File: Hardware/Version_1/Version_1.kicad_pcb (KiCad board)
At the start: 6 copper layers, 65 x 30 mm, 98 parts, among them IC1 LIFCL-40-7BG256C, IC2 W25R256JVEIQ, IC3 IS46TR16128D-125KBLA2, IC4 TPS62A01DRLR, IC5 TPS62A01DRLR, IC6 TPS62A01DRLR, J1 GPIO, J2 Conn_01x05_Pin, J3 52435-2271, J4 52435-2271, U1 CAT24C256, Y1 AK3ADDF1-156.2500T3

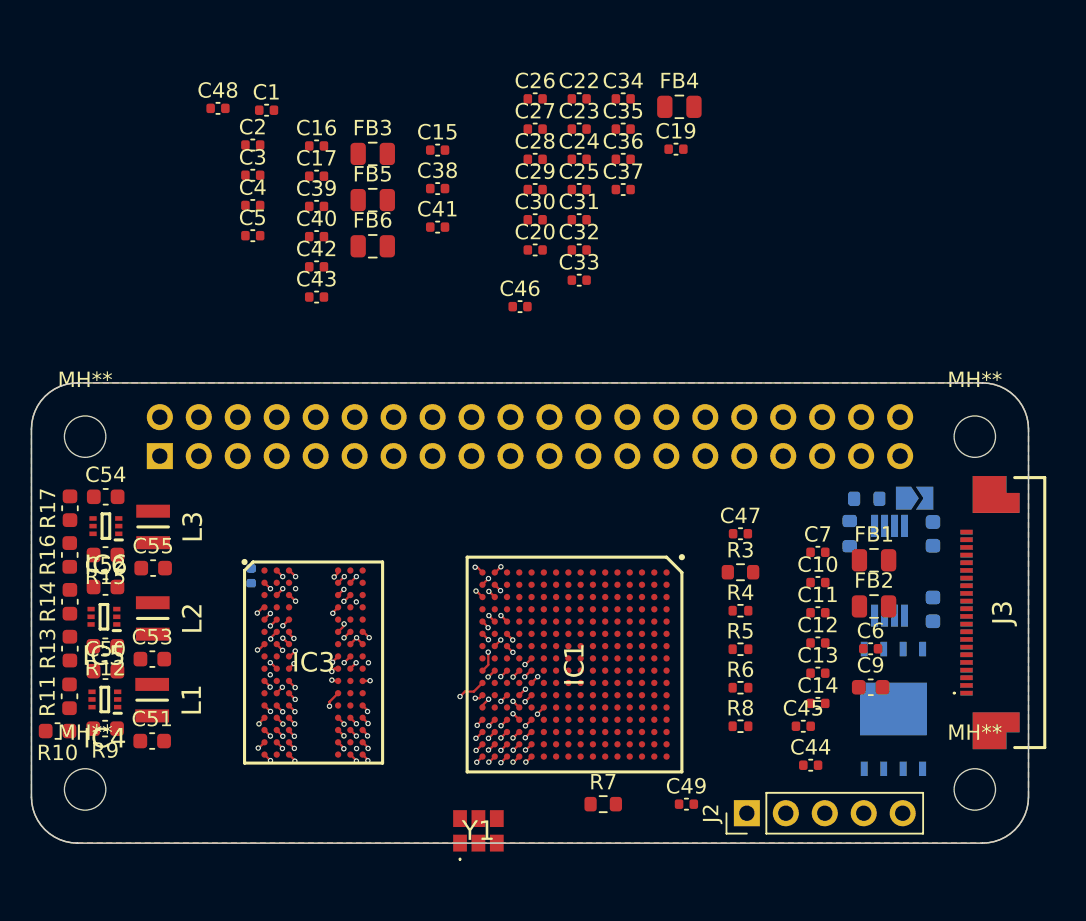
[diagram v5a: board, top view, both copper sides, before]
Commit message: mipi routing
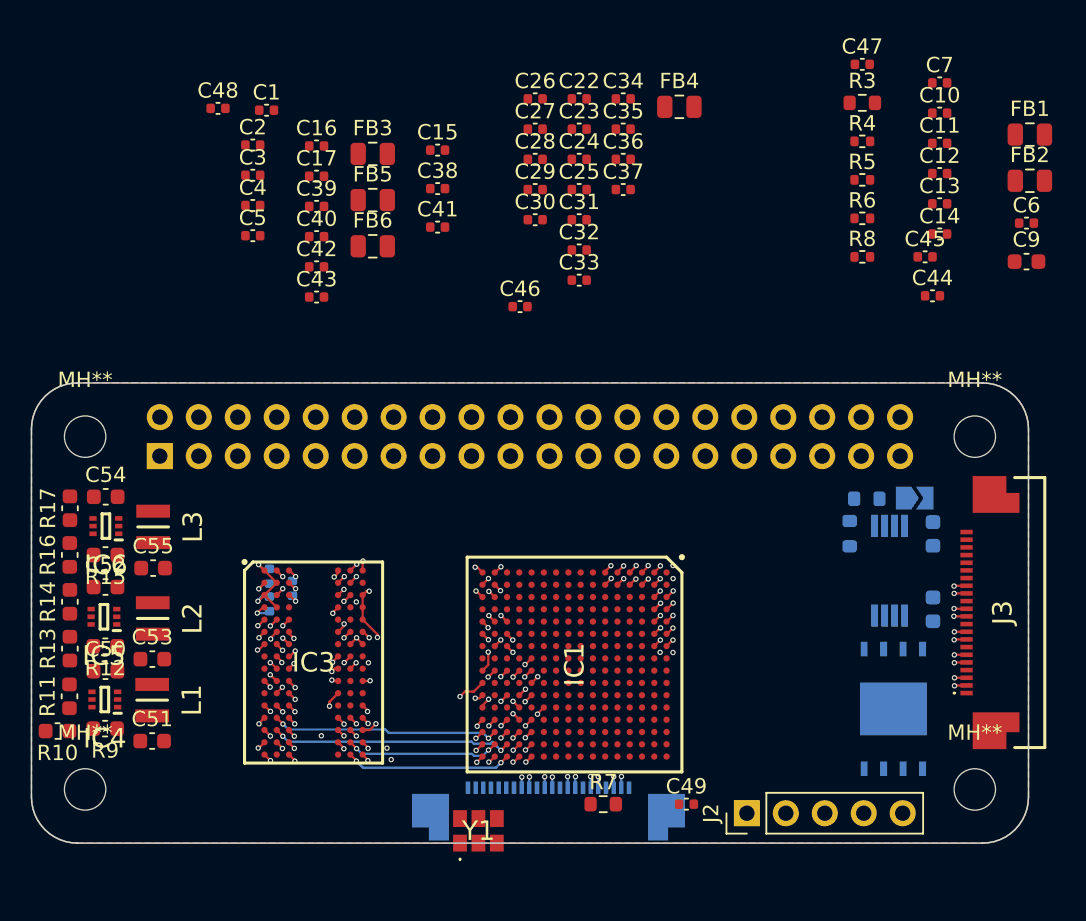
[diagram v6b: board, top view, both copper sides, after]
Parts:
- C19, C20: moved to B.Cu
- moved C19 39.8 mm to (115.5, 84.4), turned to -90 degrees
- moved J4 32.9 mm to (133.7, 98.9), turned to 180 degrees
- moved C10 31.6 mm to (159.2, 52.4)
- moved C44 31.6 mm to (158.7, 64.3)
- moved C7 31.6 mm to (159.2, 50.4)
- moved C11 31.6 mm to (159.2, 54.4)
- moved C12 31.6 mm to (159.2, 56.4)
- moved C13 31.6 mm to (159.2, 58.3)
- moved C14 31.6 mm to (159.2, 60.3)
- moved C47 31.6 mm to (154.2, 49.2)
- moved R3 31.6 mm to (154.2, 51.7)
- moved R5 31.6 mm to (154.2, 56.8)
- moved R6 31.6 mm to (154.2, 59.3)
- moved C45 31.6 mm to (158.3, 61.8)
- moved R4 31.6 mm to (154.2, 54.2)
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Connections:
- IC1 pad E1: /CSI2_D3_P -> /CSI1_D0_P
- IC1 pad E2: /CSI2_D3_P -> /CSI1_D0_N
- J3 pad 11: /CSI1_D2_N -> /CSI2_D0_N
- J3 pad 12: /CSI1_D2_P -> /CSI2_D0_P
- J3 pad 14: /CSI1_D3_N -> /CSI2_D2_N
- J3 pad 15: /CSI1_D3_P -> /CSI2_D2_P
- J3 pad 2: /CSI1_D0_N -> /CSI2_D3_N
- J3 pad 20: /CSI1_SCL -> /CSI2_SCL
- J3 pad 21: /CSI1_SDA -> /CSI2_SDA
- J3 pad 3: /CSI1_D0_P -> /CSI2_D3_P
- J3 pad 5: /CSI1_D1_N -> /CSI2_D1_N
- J3 pad 6: /CSI1_D1_P -> /CSI2_D1_P
- J3 pad 8: /CSI1_CK_N -> /CSI2_CK_N
- J3 pad 9: /CSI1_CK_P -> /CSI2_CK_P
- J4 pad 11: /CSI2_D2_N -> /CSI1_D0_N
- J4 pad 12: /CSI2_D2_P -> /CSI1_D0_P
- J4 pad 14: /CSI2_D3_N -> /CSI1_D2_N
- J4 pad 15: /CSI2_D3_P -> /CSI1_D2_P
- J4 pad 2: /CSI2_D0_N -> /CSI1_D3_N
- J4 pad 20: /CSI2_SCL -> /CSI1_SCL
- J4 pad 21: /CSI2_SDA -> /CSI1_SDA
- J4 pad 3: /CSI2_D0_P -> /CSI1_D3_P
- J4 pad 5: /CSI2_D1_N -> /CSI1_D1_N
- J4 pad 6: /CSI2_D1_P -> /CSI1_D1_P
- J4 pad 8: /CSI2_CK_N -> /CSI1_CK_N
- J4 pad 9: /CSI2_CK_P -> /CSI1_CK_P
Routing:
- net /CSI2_D3_N: track 0.00 -> 21.8 mm, vias 0 -> 2
- net /CSI2_D1_N: track 0.00 -> 21.5 mm, vias 0 -> 2
- net /CSI2_CK_N: track 0.00 -> 21.3 mm, vias 0 -> 2
- net /CSI2_D0_N: track 0.00 -> 21.0 mm, vias 0 -> 2
- net /CSI2_D2_N: track 0.00 -> 20.7 mm, vias 0 -> 2
- net /CSI2_D3_P: track 0.00 -> 20.7 mm, vias 0 -> 2
- net /CSI2_D1_P: track 0.00 -> 20.5 mm, vias 0 -> 2
- net /CSI2_CK_P: track 0.00 -> 20.2 mm, vias 0 -> 2
- net /CSI2_D0_P: track 0.00 -> 19.9 mm, vias 0 -> 2
- net /CSI2_D2_P: track 0.00 -> 19.9 mm, vias 0 -> 2
- net /CSI1_D2_P: track 0.00 -> 17.6 mm, vias 0 -> 2
- net /CSI1_D0_P: track 0.00 -> 17.3 mm, vias 0 -> 2
- net /CSI1_CK_P: track 0.00 -> 17.0 mm, vias 0 -> 2
- net /CSI1_D1_P: track 0.00 -> 16.7 mm, vias 0 -> 2
- net /CSI1_D2_N: track 0.00 -> 16.5 mm, vias 0 -> 2
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- added copper zone on In3.Cu, net /VCCDRAM

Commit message: Added i2c and flash chip
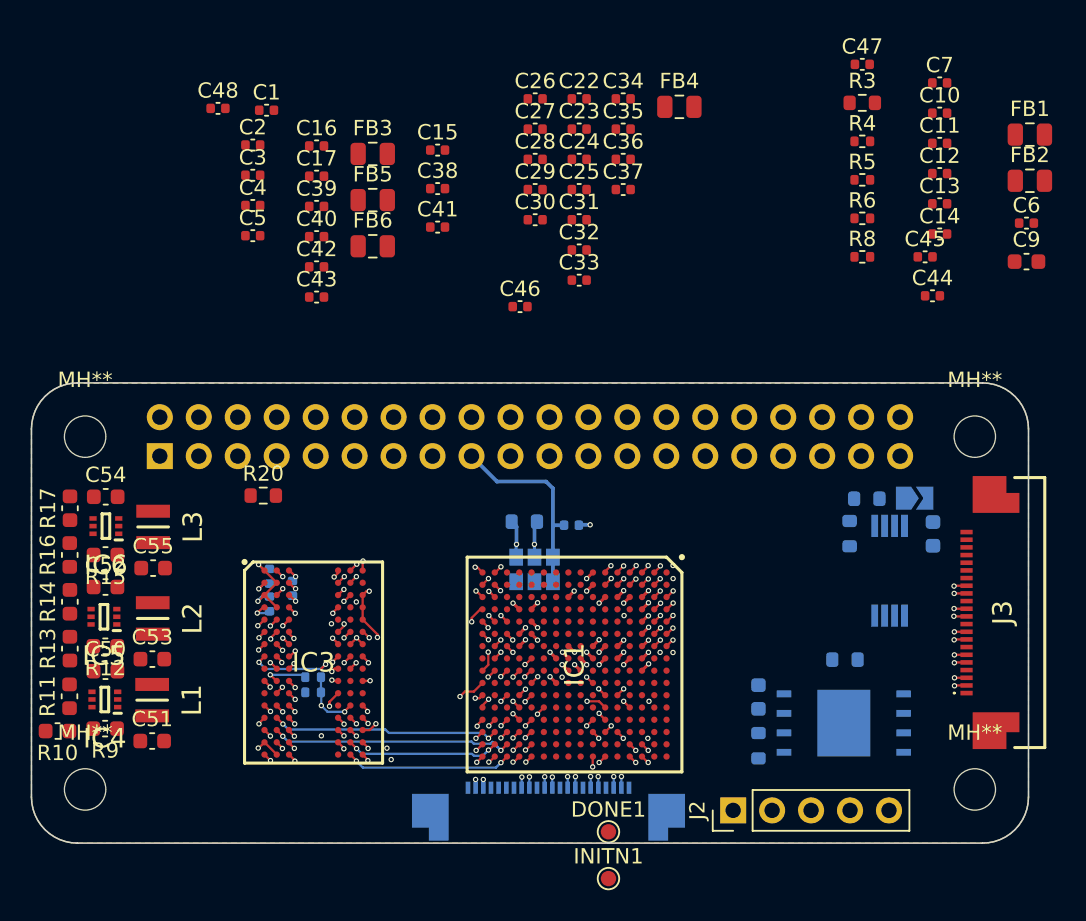
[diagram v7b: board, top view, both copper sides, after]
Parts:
- removed J1: GPIO, Connector_PinSocket_2.54mm:PinSocket_2x20_P2.54mm_Vertical
- added DONE1: TestPoint, TestPoint:TestPoint_Pad_D1.0mm, F.Cu at (137.6, 99.3)
- added INITN1: TestPoint, TestPoint:TestPoint_Pad_D1.0mm, F.Cu at (137.6, 102.3)
- added J6: GPIO, Connector_PinSocket_2.54mm:PinSocket_2x20_P2.54mm_Vertical, B.Cu at (108.4, 74.8)
- added R18: 1k0, Resistor_SMD:R_0603_1608Metric, B.Cu at (147.4, 93.7)
- added R19: 4k7, Resistor_SMD:R_0603_1608Metric, B.Cu at (153.0, 88.0)
- added R20: 4k7, Resistor_SMD:R_0603_1608Metric, F.Cu at (115.1, 77.3)
- added R21: 10k0, Resistor_SMD:R_0402_1005Metric, B.Cu at (118.4, 89.2)
- added R22: 10k0, Resistor_SMD:R_0402_1005Metric, B.Cu at (118.4, 90.2)
- C49, R7, Y1: moved to B.Cu
- moved C49 19.7 mm to (135.2, 79.3)
- moved R7 19.1 mm to (132.1, 79.0), turned to 180 degrees
- moved Y1 17.4 mm to (132.8, 82.2), turned to 180 degrees
- moved C18 12.7 mm to (147.4, 90.5), turned to -90 degrees
- moved IC2 3.37 mm to (153.0, 92.2), turned to 180 degrees
- moved J2 0.91 mm to (145.7, 97.9)
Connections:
- C49 pad 1: GND -> +3V3
- C49 pad 2: Net-(Y1-SUPPLY_VOLTAGE_(VDD)) -> GND
- IC1 pad B16: unconnected-(IC1-PT76B-PadB16) -> /DONE
- IC1 pad C12: unconnected-(IC1-PT74B-PadC12) -> /PROGRAMN
- IC1 pad C14: unconnected-(IC1-PT78B-PadC14) -> /MD0
- IC1 pad C15: unconnected-(IC1-PT78A-PadC15) -> /MCSN
- IC1 pad C16: unconnected-(IC1-PT76A-PadC16) -> /MCLK
- IC1 pad D11: unconnected-(IC1-PT74A-PadD11) -> /INITN
- IC1 pad D12: unconnected-(IC1-PT82A-PadD12) -> /MD3
- IC1 pad D15: unconnected-(IC1-PT80B-PadD15) -> /MD2
- IC1 pad D16: unconnected-(IC1-PT80A-PadD16) -> /MD1
- IC1 pad F16: unconnected-(IC1-PR19A-PadF16) -> /CSI2_SDA
- IC1 pad G10: unconnected-(IC1-PR11B-PadG10) -> /SLAVE_I2C_SCL
- IC1 pad G13: unconnected-(IC1-PR17A-PadG13) -> /CSI1_SCL
- IC1 pad G14: unconnected-(IC1-PR17B-PadG14) -> /CSI1_SDA
- IC1 pad G16: unconnected-(IC1-PR19B-PadG16) -> /CSI2_SCL
- IC1 pad G9: unconnected-(IC1-PR11A-PadG9) -> /SLAVE_I2C_SDA
- IC1 pad M4: unconnected-(IC1-PB6B-PadM4) -> /REFCLK_N
- IC1 pad N4: unconnected-(IC1-PB6A-PadN4) -> /REFCLK_P
- IC1 pad R8: unconnected-(IC1-PB42A-PadR8) -> /DML
- IC1 pad T4: unconnected-(IC1-PB20B-PadT4) -> /DMU
- IC2 pad 1: unconnected-(IC2-~{CS}-Pad1) -> /MCSN
- IC2 pad 2: unconnected-(IC2-IO1-Pad2) -> /MD1
- IC2 pad 3: unconnected-(IC2-IO2-Pad3) -> /MD2
- IC2 pad 5: unconnected-(IC2-IO0-Pad5) -> /MD0
- IC2 pad 6: unconnected-(IC2-CLK-Pad6) -> /MCLK
- IC2 pad 7: unconnected-(IC2-IO3-Pad7) -> /MD3
- IC3 pad D3: unconnected-(IC3-DMU-PadD3) -> /DMU
- IC3 pad E7: unconnected-(IC3-DML-PadE7) -> /DML
- IC3 pad H1: unconnected-(IC3-VREFDQ-PadH1) -> /DRAM_VREF
- IC3 pad M8: unconnected-(IC3-VREFCA-PadM8) -> /DRAM_VREF
- IC3 pad T2: unconnected-(IC3-RESET#-PadT2) -> /VCCDRAM
- R7 pad 1: Net-(Y1-COMPLEMENTARY_OUTPUT) -> /REFCLK_N
- R7 pad 2: Net-(Y1-OUTPUT) -> /REFCLK_P
- Y1 pad 4: Net-(Y1-OUTPUT) -> /REFCLK_P
- Y1 pad 5: Net-(Y1-COMPLEMENTARY_OUTPUT) -> /REFCLK_N
- Y1 pad 6: Net-(Y1-SUPPLY_VOLTAGE_(VDD)) -> +3V3
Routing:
- net /DML: track 0.00 -> 18.5 mm, vias 0 -> 2
- net /DMU: track 0.00 -> 17.1 mm, vias 0 -> 2
- net +3V3: track 0.00 -> 13.6 mm, vias 0 -> 1
- net GND: track 14.2 -> 27.1 mm, vias 28 -> 51
- net /CSI1_SDA: track 0.00 -> 10.5 mm, vias 0 -> 2
- net /DRAM_VREF: track 0.00 -> 9.77 mm, vias 0 -> 4
- net /CSI1_SCL: track 0.00 -> 9.38 mm, vias 0 -> 2
- net /REFCLK_P: track 0.00 -> 7.31 mm, vias 0 -> 2
- net /REFCLK_N: track 0.00 -> 7.25 mm, vias 0 -> 2
- net /VCCDRAM: track 14.4 -> 19.0 mm, vias 13 -> 14
- net /VCCAUX: track 0.00 -> 2.86 mm, vias 0 -> 5
- net /VCCDPHY: track 0.00 -> 1.18 mm, vias 0 -> 2
- net /VCCADPHY: track 0.00 -> 1.17 mm, vias 0 -> 2
- net /CSI2_SCL: track 0.00 -> 0.68 mm, vias 0 -> 1
- net /JTAG_TDI: track 0.00 -> 0.59 mm, vias 0 -> 1
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
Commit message: Layout for JTAG
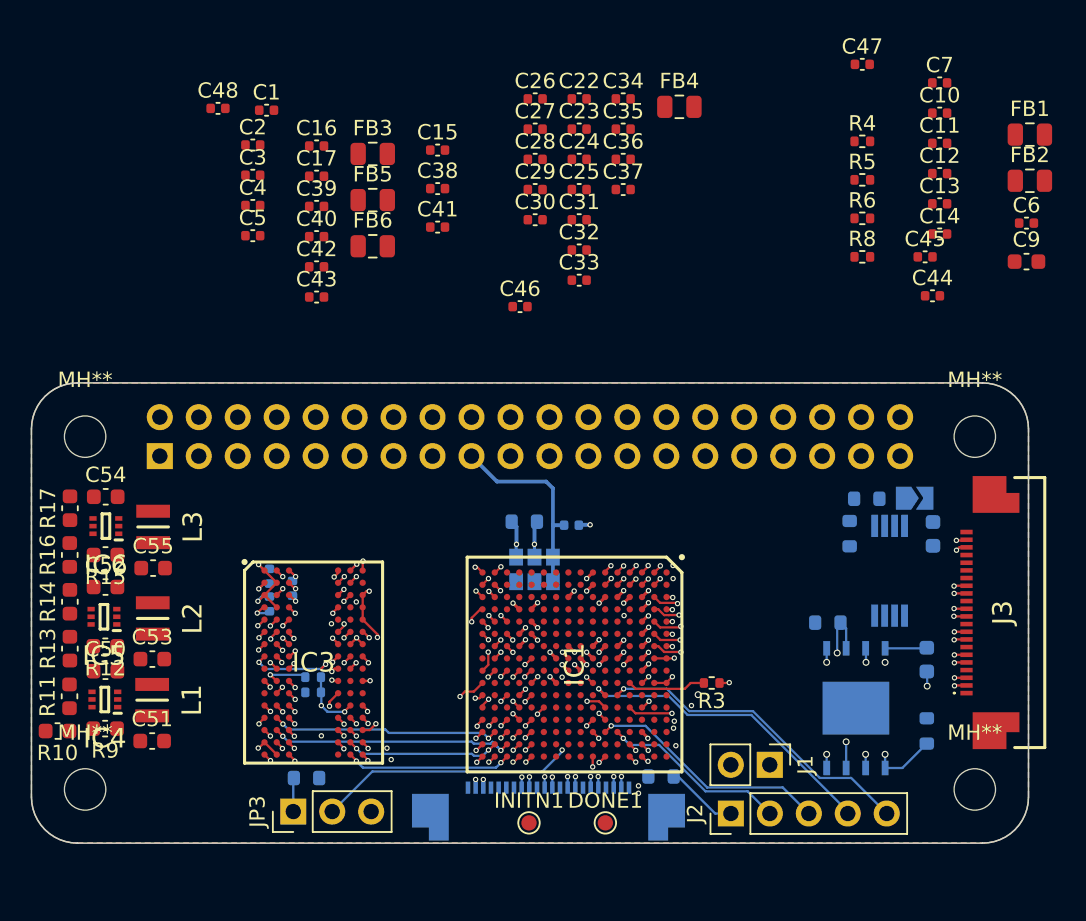
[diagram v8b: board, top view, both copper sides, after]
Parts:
- added J1: Conn_01x02_Pin, Connector_PinHeader_2.54mm:PinHeader_1x02_P2.54mm_Vertical, F.Cu at (148.1, 94.9)
- added JP3: Jumper_3_Bridged12, Connector_PinHeader_2.54mm:PinHeader_1x03_P2.54mm_Vertical, F.Cu at (117.1, 97.9)
- added R23: 4k7, Resistor_SMD:R_0603_1608Metric, B.Cu at (141.0, 95.7)
- R20: moved to B.Cu
- R3: footprint Resistor_SMD:R_0603_1608Metric -> Resistor_SMD:R_0402_1005Metric
- moved R3 39.1 mm to (144.3, 89.6), turned to 180 degrees
- moved R20 18.6 mm to (117.9, 95.8), turned to 180 degrees
- moved C18 11.2 mm to (158.4, 88.0)
- moved R18 9.21 mm to (151.9, 85.6), turned to 180 degrees
- moved R19 7.08 mm to (158.4, 92.7), turned to -90 degrees
- moved INITN1 6.33 mm to (132.4, 98.7)
- moved IC2 1.25 mm to (153.7, 91.2), turned to 90 degrees
- moved DONE1 0.62 mm to (137.4, 98.7)
- moved J2 0.25 mm to (145.6, 98.1)
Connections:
- C18 pad 1: +3.3V -> +3V3
- IC1 pad L10: /A2 -> unconnected-(IC1-PB80B-PadL10)
- IC2 pad 8: +3.3V -> +3V3
- J2 pad 1: /JTAG_TDI -> Net-(J2-Pin_1)
- J2 pad 3: /JTAG_TMS -> /JTAG_TCK
- J2 pad 4: /JTAG_TCK -> /JTAG_TDI
- J2 pad 5: unconnected-(J2-Pin_5-Pad5) -> /JTAG_TMS
- J3 pad 22: +3.3V -> +3V3
- J4 pad 22: +3.3V -> +3V3
- J6 pad 7: /PROGRAMN -> unconnected-(J6-GPIO4/GPCLK0-Pad7)
- R19 pad 1: +3.3V -> +3V3
- R20 pad 1: +3.3V -> +3V3
- R20 pad 2: /PROGRAMN -> Net-(JP3-A)
- R3 pad 1: +3V3 -> /JTAG_EN
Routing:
- net /CSI2_SDA: track 0.56 -> 40.5 mm, vias 1 -> 3
- net /CSI2_SCL: track 0.68 -> 40.5 mm, vias 1 -> 3
- net /PROGRAMN: track 0.00 -> 24.3 mm, vias 1 -> 2
- net /MCSN: track 0.57 -> 21.9 mm, vias 1 -> 3
- net /JTAG_TMS: track 0.58 -> 21.1 mm
- net /JTAG_TDI: track 0.59 -> 20.8 mm
- net /MCLK: track 0.56 -> 20.4 mm, vias 1 -> 3
- net /MD1: track 0.55 -> 18.3 mm, vias 1 -> 3
- net /MD3: track 0.57 -> 17.9 mm, vias 1 -> 2
- net /MD2: track 0.56 -> 17.3 mm, vias 1 -> 3
- net /CSI1_D3_P: track 1.32 -> 17.3 mm
- net /MD0: track 0.00 -> 15.5 mm, vias 0 -> 3
- net /JTAG_TCK: track 0.56 -> 15.8 mm
- net /CSI1_D3_N: track 1.28 -> 16.2 mm
- net /JTAG_TDO: track 0.57 -> 12.2 mm
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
